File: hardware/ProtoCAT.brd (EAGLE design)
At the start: 59.7 x 53.3 mm, 54 parts, among them U1 ARDUINO, U3 TB6612FNG

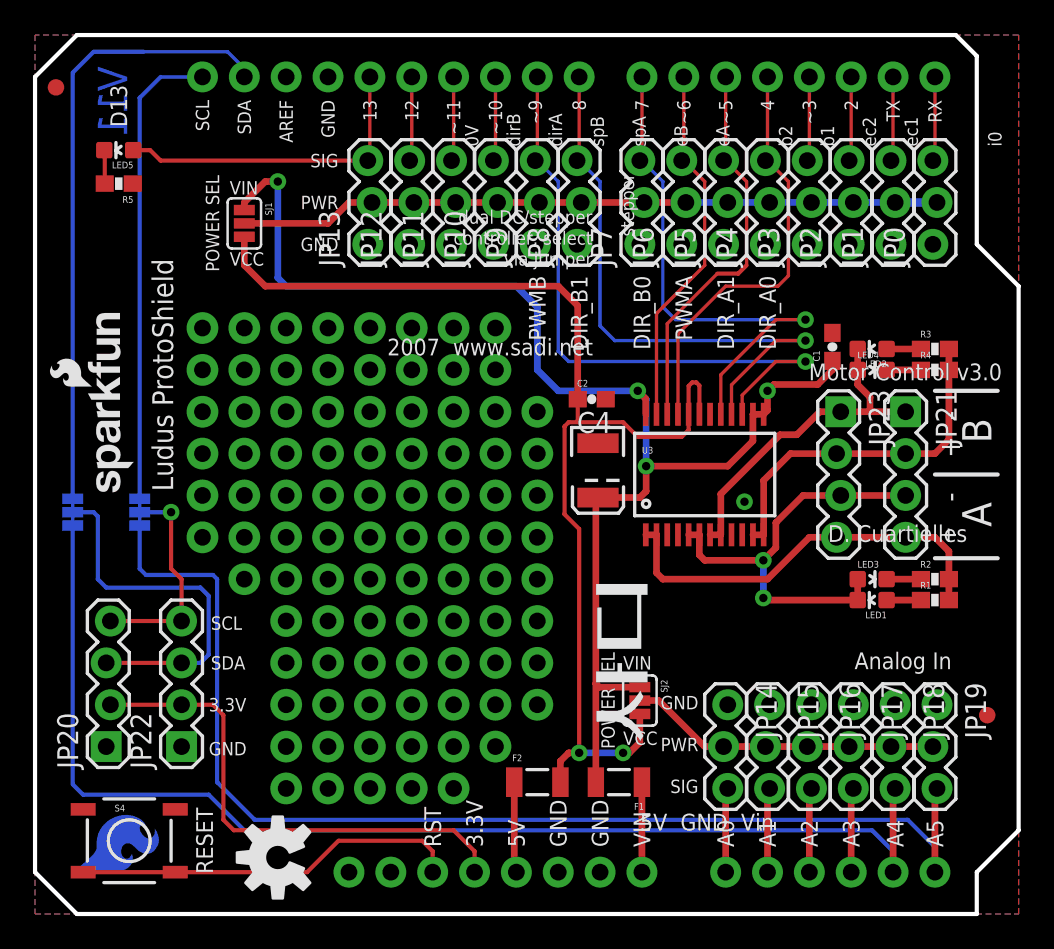
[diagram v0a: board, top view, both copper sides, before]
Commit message: Changed layout of shield to include staggered locking holes
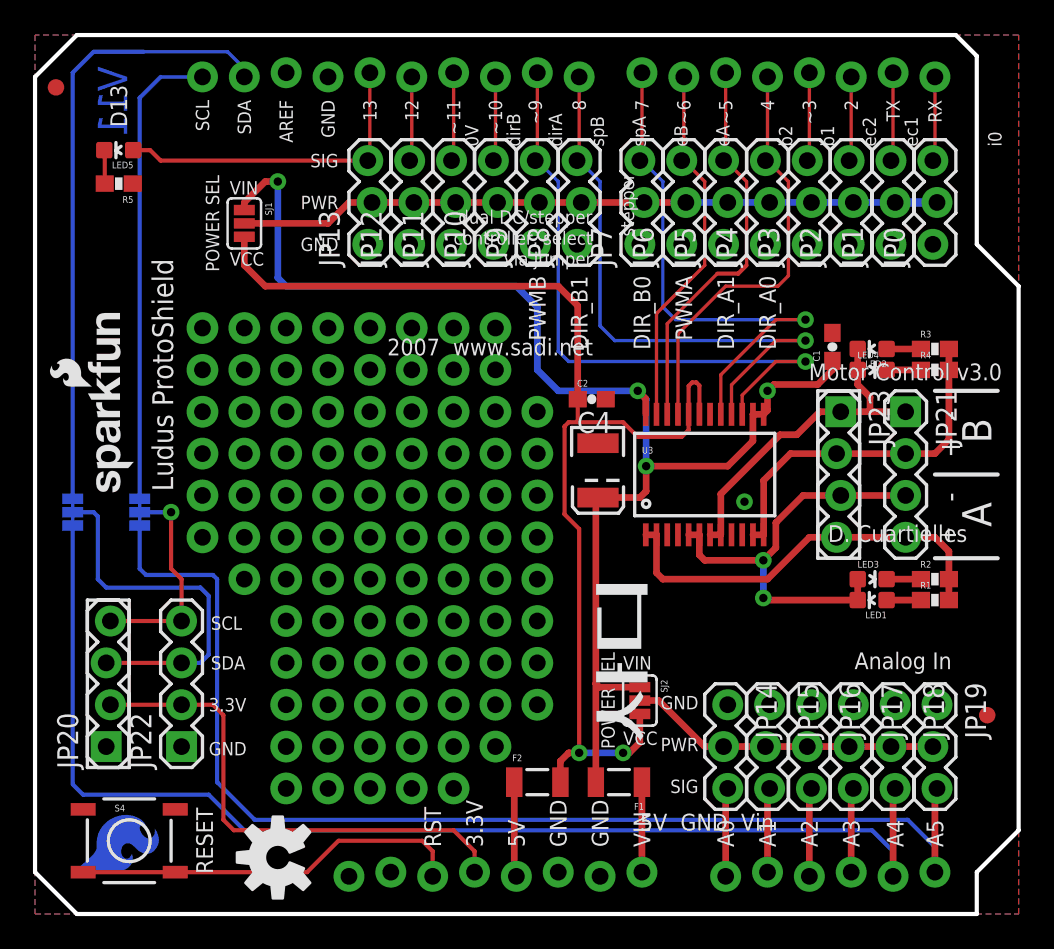
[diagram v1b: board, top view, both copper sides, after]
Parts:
- U1: device SparkFun-Boards:UNO_R3_SHIELD_NOLABELS -> SparkFun-Boards:UNO_R3_SHIELD_NOLABELS_LOCK
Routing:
- net A4: track 73.6 -> 74.1 mm
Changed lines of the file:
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@@
 <text x="40.132" y="12.827" size="0.8128" layer="22" font="vector" ratio="15" rot="MR0" align="center-left">GND</text>
 <text x="40.132" y="7.747" size="0.8128" layer="22" font="vector" ratio="15" rot="MR0" align="center-left">SIG</text>
+<wire x1="47.498" y1="21.59" x2="50.038" y2="21.59" width="0.2032" layer="21"/>
+<wire x1="50.038" y1="21.59" x2="50.038" y2="31.75" width="0.2032" layer="21"/>
+<wire x1="50.038" y1="31.75" x2="47.498" y2="31.75" width="0.2032" layer="21"/>
+<wire x1="47.498" y1="31.75" x2="47.498" y2="21.59" width="0.2032" layer="21"/>
+<wire x1="3.175" y1="8.89" x2="5.715" y2="8.89" width="0.2032" layer="21"/>
+<wire x1="5.715" y1="8.89" x2="5.715" y2="19.05" width="0.2032" layer="21"/>
+<wire x1="5.715" y1="19.05" x2="3.175" y2="19.05" width="0.2032" layer="21"/>
+<wire x1="3.175" y1="19.05" x2="3.175" y2="8.89" width="0.2032" layer="21"/>
 </plain>
 <attributes>
@@
 <attribute name="VALUE" x="49.403" y="33.0835" size="0.4064" layer="27" rot="R180"/>
 </element>
-<element name="U1" library="SparkFun-Boards" package="UNO_R3_SHIELD_NOLABELS" value="ARDUINO" x="0" y="53.34" rot="R270"/>
+<element name="U1" library="SparkFun-Boards" package="UNO_R3_SHIELD_NOLABELS_LOCK" value="ARDUINO" x="0" y="53.34" rot="R270"/>
 <element name="JP0" library="SparkFun-Connectors" package="1X03_LOCK" value="D0" x="54.61" y="40.64" rot="R90"/>
 <element name="JP1" library="SparkFun-Connectors" package="1X03_LOCK" value="D1" x="52.07" y="40.64" rot="R90"/>
@@
 <element name="LOGO3" library="SparkFun-Aesthetics" package="SFE_LOGO_FLAME_COPPER_.2" value="SFE_LOGO_FLAME.2COP" x="2.159" y="2.286" rot="SMR90"/>
 <element name="LOGO4" library="SparkFun-Aesthetics" package="SFE_LOGO_NAME_FLAME_.1" value="SFE_LOGO_NAME_FLAME.1_INCH" x="6.858" y="43.688" rot="MR270"/>
-<element name="JP23" library="SparkFun-Connectors" package="1X04_LOCK" value="" x="48.768" y="30.48" rot="R270"/>
+<element name="JP23" library="SparkFun-Connectors" package="1X04_LOCK" value="" x="48.768" y="30.48" smashed="yes" rot="R270">
+<attribute name="NAME" x="50.5968" y="31.8262" size="1.27" layer="25" ratio="10" rot="R270"/>
+<attribute name="VALUE" x="45.593" y="31.75" size="1.27" layer="27" rot="R270"/>
+</element>
 </elements>
 <signals>
@@
 <wire x1="6.985" y1="46.355" x2="7.62" y2="45.72" width="0.254" layer="1"/>
 <wire x1="20.193" y1="45.72" x2="7.62" y2="45.72" width="0.254" layer="1"/>
-<wire x1="20.32" y1="50.8" x2="20.32" y2="45.847" width="0.2032" layer="1"/>
+<wire x1="20.32" y1="51.054" x2="20.32" y2="45.847" width="0.2032" layer="1"/>
 <wire x1="20.32" y1="45.847" x2="20.193" y2="45.72" width="0.2032" layer="1"/>
 </signal>
@@
 <wire x1="32.385" y1="33.528" x2="31.75" y2="34.163" width="0.2032" layer="16"/>
 <wire x1="32.385" y1="33.528" x2="46.755" y2="33.528" width="0.2032" layer="16"/>
-<wire x1="30.48" y1="50.8" x2="30.48" y2="45.847" width="0.2032" layer="1"/>
+<wire x1="30.48" y1="51.054" x2="30.48" y2="45.847" width="0.2032" layer="1"/>
 <wire x1="30.48" y1="45.847" x2="30.353" y2="45.72" width="0.2032" layer="1"/>
 <wire x1="30.353" y1="45.72" x2="30.48" y2="45.72" width="0.2032" layer="16"/>
@@
 <contactref element="U1" pad="5V"/>
 <contactref element="F2" pad="1"/>
-<wire x1="29.08" y1="8.001" x2="29.08" y2="2.67" width="0.4064" layer="1"/>
-<wire x1="29.08" y1="2.67" x2="29.21" y2="2.54" width="0.4064" layer="1"/>
+<wire x1="29.08" y1="8.001" x2="29.08" y2="2.416" width="0.4064" layer="1"/>
+<wire x1="29.08" y1="2.416" x2="29.21" y2="2.286" width="0.4064" layer="1"/>
 </signal>
 <signal name="D10">
@@
 <contactref element="U1" pad="A4"/>
 <contactref element="JP18" pad="3"/>
-<wire x1="52.07" y1="3.81" x2="52.07" y2="2.54" width="0.254" layer="16"/>
+<wire x1="52.07" y1="3.81" x2="52.07" y2="2.286" width="0.254" layer="16"/>
 <wire x1="52.07" y1="3.81" x2="50.8" y2="5.08" width="0.254" layer="16"/>
 <contactref element="SJ3" pad="3"/>
 <wire x1="12.7" y1="5.08" x2="50.8" y2="5.08" width="0.254" layer="16"/>
-<wire x1="52.07" y1="2.54" x2="52.07" y2="7.493" width="0.4064" layer="1"/>
+<wire x1="52.07" y1="2.286" x2="52.07" y2="7.493" width="0.4064" layer="1"/>
 <wire x1="52.07" y1="7.493" x2="52.197" y2="7.62" width="0.4064" layer="1"/>
 <wire x1="2.286" y1="23.5712" x2="2.286" y2="7.874" width="0.254" layer="16"/>
@@
 <contactref element="U1" pad="A2"/>
 <contactref element="JP16" pad="3"/>
-<wire x1="46.99" y1="2.54" x2="46.99" y2="7.493" width="0.4064" layer="1"/>
+<wire x1="46.99" y1="2.286" x2="46.99" y2="7.493" width="0.4064" layer="1"/>
 <wire x1="46.99" y1="7.493" x2="47.117" y2="7.62" width="0.4064" layer="1"/>
 </signal>
@@
 <contactref element="U1" pad="A0"/>
 <contactref element="JP14" pad="3"/>
-<wire x1="41.91" y1="2.54" x2="41.91" y2="7.493" width="0.4064" layer="1"/>
+<wire x1="41.91" y1="2.286" x2="41.91" y2="7.493" width="0.4064" layer="1"/>
 <wire x1="41.91" y1="7.493" x2="42.037" y2="7.62" width="0.4064" layer="1"/>
 </signal>
@@
 <wire x1="38.862" y1="36.068" x2="38.1" y2="36.83" width="0.2032" layer="16"/>
 <wire x1="38.1" y1="36.83" x2="38.1" y2="44.45" width="0.2032" layer="16"/>
-<wire x1="36.83" y1="50.8" x2="36.83" y2="45.847" width="0.2032" layer="1"/>
+<wire x1="36.83" y1="51.054" x2="36.83" y2="45.847" width="0.2032" layer="1"/>
 <wire x1="36.83" y1="45.847" x2="36.703" y2="45.72" width="0.2032" layer="1"/>
 <wire x1="36.703" y1="45.72" x2="36.83" y2="45.72" width="0.2032" layer="16"/>
@@
 <wire x1="43.18" y1="39.37" x2="42.672" y2="38.862" width="0.254" layer="1"/>
 <wire x1="42.672" y1="38.862" x2="41.402" y2="38.862" width="0.254" layer="1"/>
-<wire x1="41.91" y1="50.8" x2="41.91" y2="45.847" width="0.2032" layer="1"/>
+<wire x1="41.91" y1="51.054" x2="41.91" y2="45.847" width="0.2032" layer="1"/>
 <wire x1="41.91" y1="45.847" x2="41.783" y2="45.72" width="0.2032" layer="1"/>
 <wire x1="41.783" y1="45.72" x2="41.91" y2="45.72" width="0.2032" layer="1"/>
@@
 <contactref element="U1" pad="D11"/>
 <contactref element="JP11" pad="3"/>
-<wire x1="25.4" y1="50.8" x2="25.4" y2="45.847" width="0.2032" layer="1"/>
+<wire x1="25.4" y1="51.054" x2="25.4" y2="45.847" width="0.2032" layer="1"/>
 <wire x1="25.4" y1="45.847" x2="25.273" y2="45.72" width="0.2032" layer="1"/>
 </signal>
@@
 <contactref element="JP1" pad="3"/>
 <contactref element="U1" pad="TX"/>
-<wire x1="52.07" y1="50.8" x2="52.07" y2="45.847" width="0.2032" layer="1"/>
+<wire x1="52.07" y1="51.054" x2="52.07" y2="45.847" width="0.2032" layer="1"/>
 <wire x1="52.07" y1="45.847" x2="51.943" y2="45.72" width="0.2032" layer="1"/>
 </signal>
@@
 <wire x1="8.509" y1="2.54" x2="2.921" y2="2.54" width="0.254" layer="1"/>
 <wire x1="8.509" y1="2.54" x2="16.51" y2="2.54" width="0.254" layer="1"/>
-<wire x1="24.13" y1="3.81" x2="24.13" y2="2.54" width="0.254" layer="1"/>
+<wire x1="24.13" y1="3.81" x2="24.13" y2="2.286" width="0.254" layer="1"/>
 <wire x1="24.13" y1="3.81" x2="23.495" y2="4.445" width="0.254" layer="1"/>
 <wire x1="23.495" y1="4.445" x2="18.415" y2="4.445" width="0.254" layer="1"/>
@@
 <contactref element="U1" pad="D3"/>
 <contactref element="JP3" pad="3"/>
-<wire x1="46.99" y1="50.8" x2="46.99" y2="45.847" width="0.2032" layer="1"/>
+<wire x1="46.99" y1="51.054" x2="46.99" y2="45.847" width="0.2032" layer="1"/>
 <wire x1="46.99" y1="45.847" x2="46.863" y2="45.72" width="0.2032" layer="1"/>
 </signal>
